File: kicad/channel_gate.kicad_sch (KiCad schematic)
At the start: 17 parts, among them U4 7UL2G00FK, U401 74LVC1G02W5, U402 74LVC1G80GW, U404 74LVC1G80GW, U5 74LVC1G157, U6 7UL2G00FK, U7 7UL2G00FK

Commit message: replace alum caps with ceramics, change mpn labeling
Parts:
- CD4, CD402, CD404, CD406, CD5, CD6: MPN (none) -> KGM05AR51C104KH; Supplier https://www.digikey.com/en/products/detail/kyocera-avx/KGM0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 -> (none)
- CD401, CD403, CD405: MPN (none) -> CC0402JRNPO9BN101; Supplier https://www.digikey.com/en/products/detail/yageo/CC0402JRNP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 -> (none)
- U401: MPN (none) -> 74LVC1G02W5-7; Supplier https://www.digikey.com/en/products/detail/diodes-incorpora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 -> (none)
- U402, U404: MPN (none) -> 74LVC1G80GW,125; Supplier https://www.digikey.com/en/products/detail/nexperia-usa-inc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 -> (none)
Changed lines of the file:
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@@
 			)
 		)
-		(property "Supplier" "https://www.digikey.com/en/products/detail/kyocera-avx/KGM05AR51C104KH/563236"
+		(property "Supplier" ""
+			(at 161.29 110.49 0)
+			(effects
+				(font
+					(size 1.27 1.27)
+				)
+				(hide yes)
+			)
+		)
+		(property "MPN" "KGM05AR51C104KH"
 			(at 161.29 110.49 0)
 			(effects
@@
 			)
 		)
-		(property "Supplier" "https://www.digikey.com/en/products/detail/yageo/CC0402JRNPO9BN101/302758"
+		(property "Supplier" ""
+			(at 115.57 110.49 0)
+			(effects
+				(font
+					(size 1.27 1.27)
+				)
+				(hide yes)
+			)
+		)
+		(property "MPN" "CC0402JRNPO9BN101"
 			(at 115.57 110.49 0)
 			(effects
@@
 			)
 		)
-		(property "Supplier" "https://www.digikey.com/en/products/detail/diodes-incorporated/74LVC1G02W5-7/2330097"
+		(property "Supplier" ""
+			(at 43.18 137.16 0)
+			(effects
+				(font
+					(size 1.27 1.27)
+				)
+				(hide yes)
+			)
+		)
+		(property "MPN" "74LVC1G02W5-7"
 			(at 43.18 137.16 0)
 			(effects
@@
 			)
 		)
-		(property "Supplier" "https://www.digikey.com/en/products/detail/kyocera-avx/KGM05AR51C104KH/563236"
+		(property "Supplier" ""
+			(at 130.81 110.49 0)
+			(effects
+				(font
+					(size 1.27 1.27)
+				)
+				(hide yes)
+			)
+		)
+		(property "MPN" "KGM05AR51C104KH"
 			(at 130.81 110.49 0)
 			(effects
@@
 			)
 		)
-		(property "Supplier" "https://www.digikey.com/en/products/detail/yageo/CC0402JRNPO9BN101/302758"
+		(property "Supplier" ""
+			(at 146.05 110.49 0)
+			(effects
+				(font
+					(size 1.27 1.27)
+				)
+				(hide yes)
+			)
+		)
+		(property "MPN" "CC0402JRNPO9BN101"
 			(at 146.05 110.49 0)
 			(effects
@@
 			)
 		)
-		(property "Supplier" "https://www.digikey.com/en/products/detail/kyocera-avx/KGM05AR51C104KH/563236"
+		(property "Supplier" ""
+			(at 203.2 110.49 0)
+			(effects
+				(font
+					(size 1.27 1.27)
+				)
+				(hide yes)
+			)
+		)
+		(property "MPN" "KGM05AR51C104KH"
 			(at 203.2 110.49 0)
 			(effects
@@
 			)
 		)
-		(property "Supplier" "https://www.digikey.com/en/products/detail/kyocera-avx/KGM05AR51C104KH/563236"
+		(property "Supplier" ""
+			(at 130.81 78.74 0)
+			(effects
+				(font
+					(size 1.27 1.27)
+				)
+				(hide yes)
+			)
+		)
+		(property "MPN" "KGM05AR51C104KH"
 			(at 130.81 78.74 0)
 			(effects
@@
 			)
 		)
-		(property "Supplier" "https://www.digikey.com/en/products/detail/kyocera-avx/KGM05AR51C104KH/563236"
+		(property "Supplier" ""
+			(at 90.17 88.9 0)
+			(effects
+				(font
+					(size 1.27 1.27)
+				)
+				(hide yes)
+			)
+		)
+		(property "MPN" "KGM05AR51C104KH"
 			(at 90.17 88.9 0)
 			(effects
@@
 			)
 		)
-		(property "Supplier" "https://www.digikey.com/en/products/detail/nexperia-usa-inc/74LVC1G80GW-125/1231494"
+		(property "Supplier" ""
+			(at 172.72 43.18 0)
+			(effects
+				(font
+					(size 1.27 1.27)
+				)
+				(hide yes)
+			)
+		)
+		(property "MPN" "74LVC1G80GW,125"
 			(at 172.72 43.18 0)
 			(effects
@@
 			)
 		)
-		(property "Supplier" "https://www.digikey.com/en/products/detail/kyocera-avx/KGM05AR51C104KH/563236"
+		(property "Supplier" ""
+			(at 48.26 88.9 0)
+			(effects
+				(font
+					(size 1.27 1.27)
+				)
+				(hide yes)
+			)
+		)
+		(property "MPN" "KGM05AR51C104KH"
 			(at 48.26 88.9 0)
 			(effects
@@
 			)
 		)
-		(property "Supplier" "https://www.digikey.com/en/products/detail/nexperia-usa-inc/74LVC1G80GW-125/1231494"
+		(property "Supplier" ""
+			(at 133.35 43.18 0)
+			(effects
+				(font
+					(size 1.27 1.27)
+				)
+				(hide yes)
+			)
+		)
+		(property "MPN" "74LVC1G80GW,125"
 			(at 133.35 43.18 0)
 			(effects
@@
 			)
 		)
-		(property "Supplier" "https://www.digikey.com/en/products/detail/yageo/CC0402JRNPO9BN101/302758"
+		(property "Supplier" ""
 			(at 115.57 78.74 0)
 			(effects
+				(font
+					(size 1.27 1.27)
+				)
+				(hide yes)
+			)
+		)
+		(property "MPN" "CC0402JRNPO9BN101"
+			(at 115.57 78.74 0)
+			(effects

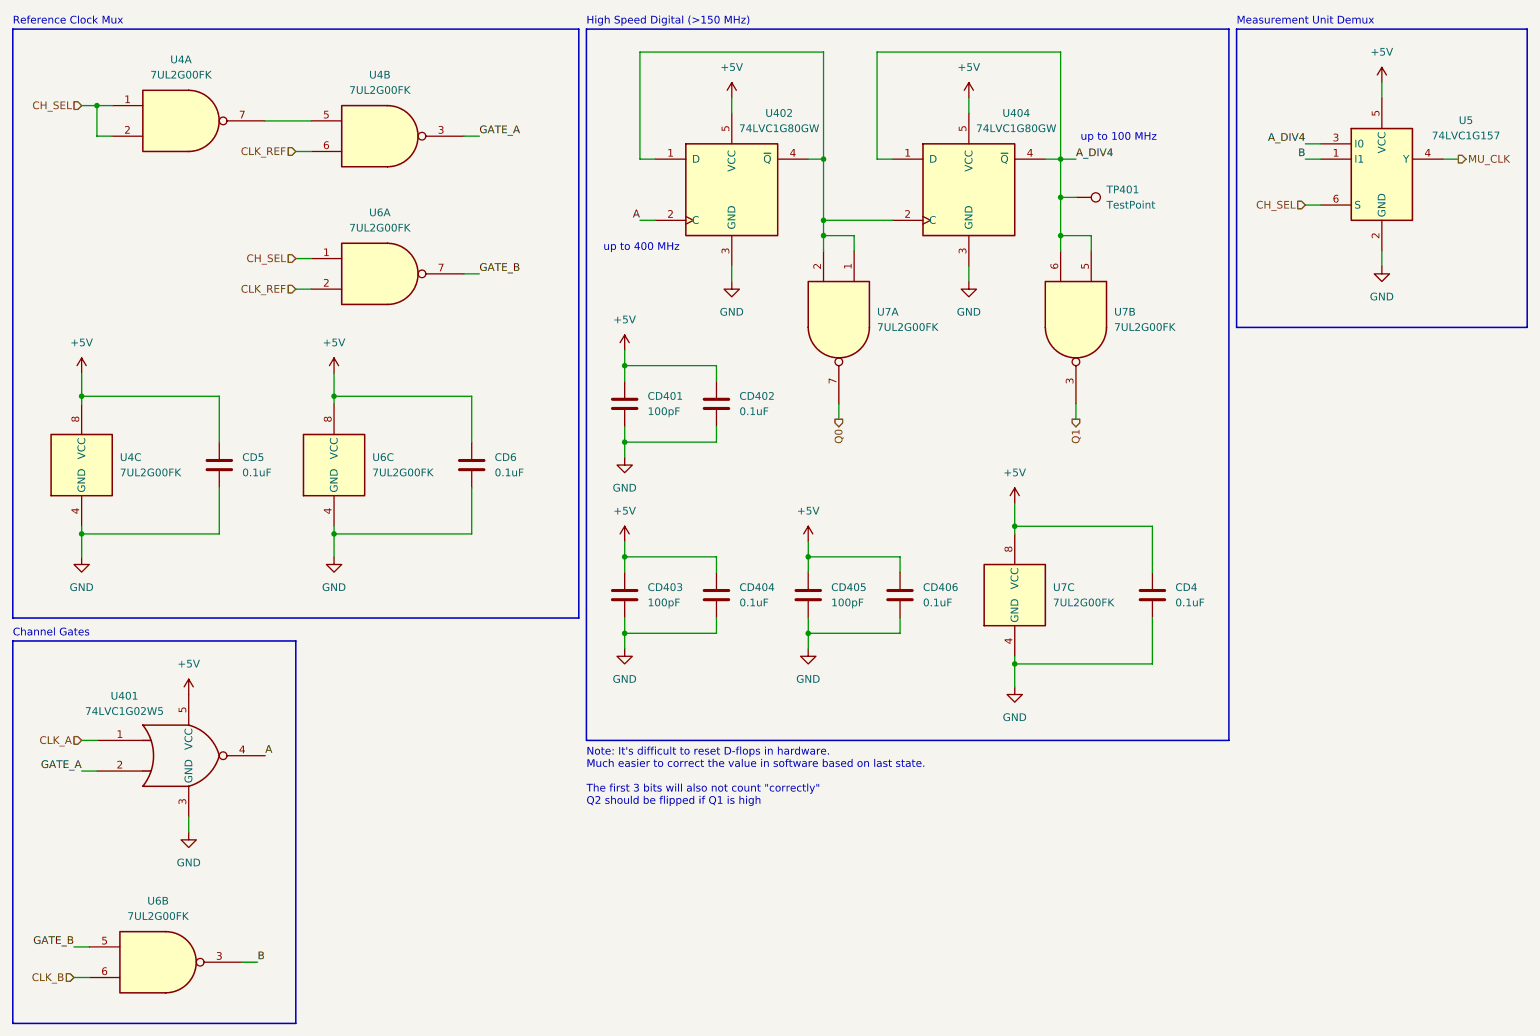
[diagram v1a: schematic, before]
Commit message: finish 2.0 part selection
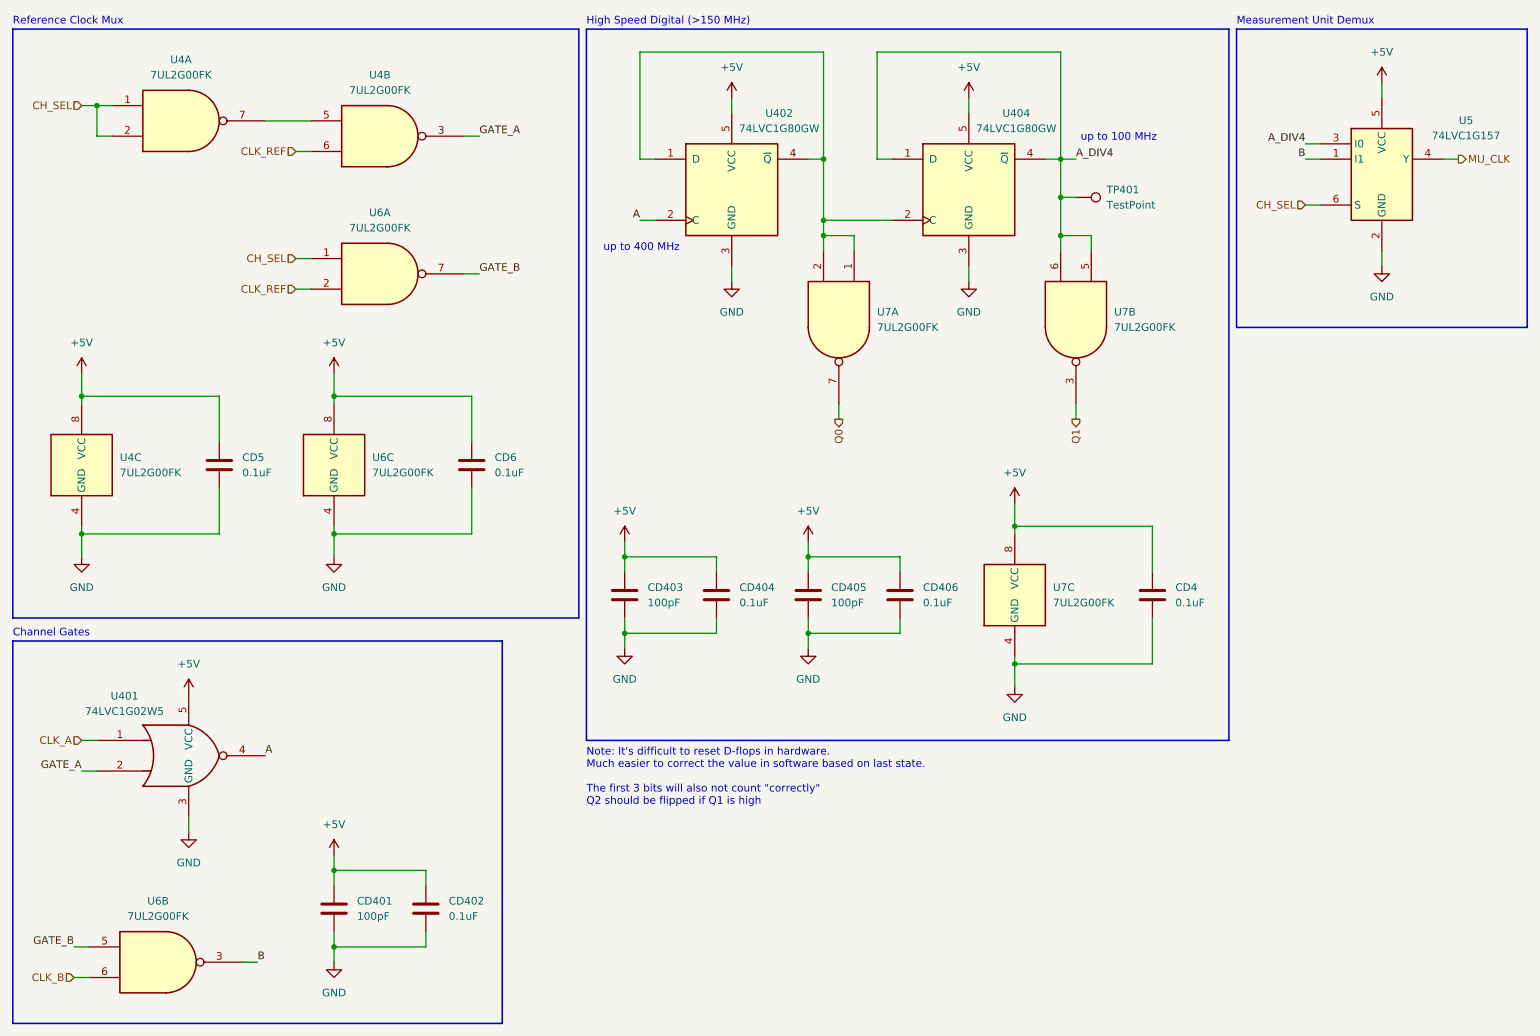
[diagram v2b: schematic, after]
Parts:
- TP401: MPN (none) -> RCWCTE; Supplier https://www.digikey.com/en/products/detail/harwin-inc/S2751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 -> (none)
- U4, U6, U7: MPN (none) -> 7UL2G00FK,LF
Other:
- moved on the sheet: CD401, CD402

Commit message: assign references
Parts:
- TP401: value TestPoint -> RCW
- renumbered CD5 to CD401, CD6 to CD402, CD401 to CD403, CD402 to CD404, CD403 to CD405, CD404 to CD406, CD405 to CD407, CD406 to CD408, CD4 to CD409, U4 to U401, U6 to U402, U401 to U403, U402 to U404, U7 to U405, U404 to U406, U5 to U407

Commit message: minor fixes, 2.0 schematic
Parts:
- TP401: footprint Custom:TestPoint_Pad_2.0x2.0mm_Fix -> Custom:TestPoint_KOA_RCW
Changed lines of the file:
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@@
 	(title_block
 		(title "Frequency Counter")
-		(date "2026-02-18")
-		(rev "2.0-draft")
+		(date "2026-02-19")
+		(rev "2.0")
 		(company "vladaviedov.org")
 		(comment 1 "Maximum Precision (125 mHz ~ 325 MHz): 62.5 mHz")
@@
 			)
 		)
-		(property "Footprint" "Custom:TestPoint_Pad_2.0x2.0mm_Fix"
+		(property "Footprint" "Custom:TestPoint_KOA_RCW"
 			(at 190.5 49.53 0)
 			(effects

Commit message: redesign pcb for 2.0
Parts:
- removed TP401: RCW, Custom:TestPoint_KOA_RCW, symbol Connector:TestPoint
- added CD410: 100pF, Custom:C_0402_1005Metric_Fix, symbol Device:C
- added CD411: 0.1uF, Custom:C_0402_1005Metric_Fix, symbol Device:C
- renumbered U406 to U405, U405 to U406
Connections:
- net +5V: now also CD410.1, CD411.1
- net A_DIV4: now also U406.1, U406.2; no longer U406.5, U406.6
- net GND: now also CD410.2, CD411.2
- net Q0: now also U406.3; no longer U406.7
- net Q1: now also U406.7; no longer U406.3
- net at U404.1 (D), U404.4 (~{Q}), U405.2 (C): now also U406.5, U406.6; no longer U406.1, U406.2
